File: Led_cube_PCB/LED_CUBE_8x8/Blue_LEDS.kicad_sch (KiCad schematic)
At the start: 101 parts, among them IC13 74AHCT244PW,118, IC14 74AHCT244PW,118, IC15 74AHCT244PW,118, IC17 74AHCT244PW,118, IC18 74AHCT244PW,118, IC23 74AHCT244PW,118, IC24 74AHCT244PW,118, IC25 74AHCT244PW,118, IC27 SN74HCS238DYYR, J7 Conn_02x16_Odd_Even, J8 Conn_02x16_Odd_Even

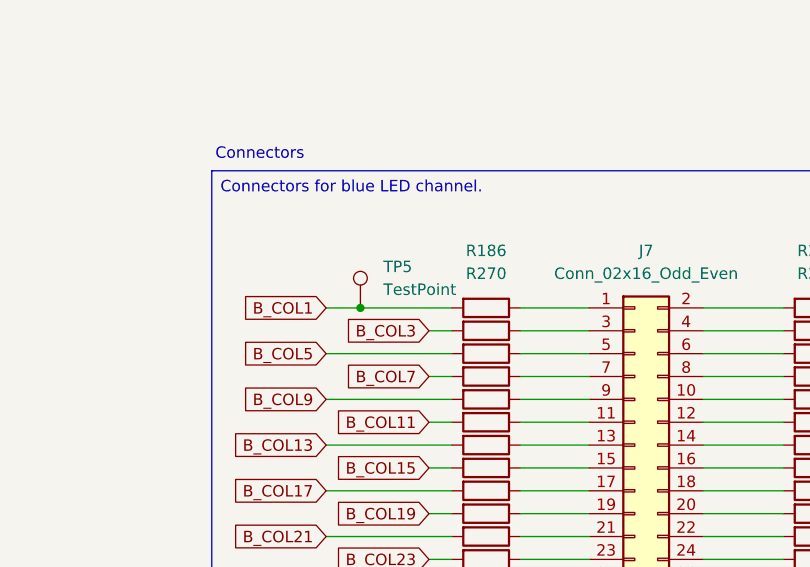
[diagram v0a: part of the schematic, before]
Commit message: Finalized schematic changed power source and buck converter due to unavailability stock mouser. Also assigned all the footprints to all components and ran ERC.
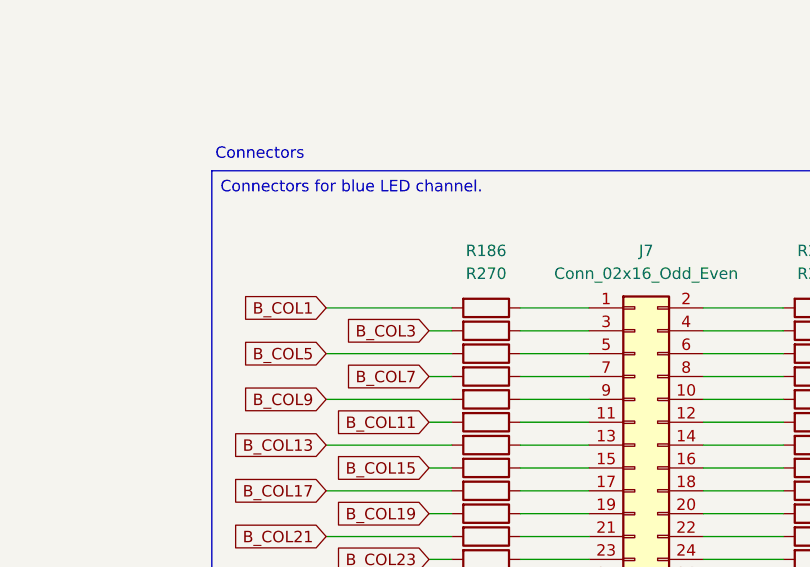
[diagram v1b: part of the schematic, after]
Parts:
- removed TP5: TestPoint, TestPoint:TestPoint_Pad_D2.0mm, symbol Connector:TestPoint
- C12, C14, C15, C20, C21, C22, C23, C24: footprint (none) -> Capacitor_SMD:C_0805_2012Metric_Pad1.18x1.45mm_HandSolder
- IC13, IC14, IC15, IC17, IC18, IC23, IC24, IC25: footprint SOP65P640X110-20N -> SamacSys_Parts:SOP65P640X110-20N
- IC27: footprint SOP50P326X110-16N -> SamacSys_Parts:SOP50P326X110-16N
- R186, R187, R188, R189, R190, R191, R192, R193, R194, R195, R196, R197, R198, R199, R200, R201, R202, R203, R204, R205, R206, R207, R208, R209, R210, R211, R212, R213, R214, R215, R216, R217, R218, R219, R220, R221, R222, R223, R224, R225, R226, R227, R228, R229, R230, R231, R232, R233, R234, R235, R236, R237, R238, R239, R240, R241, R242, R243, R244, R245, R246, R247, R248, R249, R26, R27, R28, R29, R3, R30, R33, R34, R35, R36, R45, R46, R47, R48, R49, R50, R51: footprint (none) -> Resistor_SMD:R_0805_2012Metric_Pad1.20x1.40mm_HandSolder

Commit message: start of PCB layout
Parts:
- removed R30, R33, R34, R35, R48, R49, R50, R51: R10K, Resistor_SMD:R_0805_2012Metric_Pad1.20x1.40mm_HandSolder, symbol Device:R
- C12, C14, C15, C20, C21, C22, C23, C24: footprint Capacitor_SMD:C_0805_2012Metric_Pad1.18x1.45mm_HandSolder -> Capacitor_SMD:C_0603_1608Metric_Pad1.08x0.95mm_HandSolder
- R186, R187, R188, R189, R190, R191, R192, R193, R194, R195, R196, R197, R198, R199, R200, R201, R202, R203, R204, R205, R206, R207, R208, R209, R210, R211, R212, R213, R214, R215, R216, R217, R218, R219, R220, R221, R222, R223, R224, R225, R226, R227, R228, R229, R230, R231, R232, R233, R234, R235, R236, R237, R238, R239, R240, R241, R242, R243, R244, R245, R246, R247, R248, R249, R26, R27, R28, R29, R3, R36, R45, R46, R47: footprint Resistor_SMD:R_0805_2012Metric_Pad1.20x1.40mm_HandSolder -> Resistor_SMD:R_0603_1608Metric_Pad0.98x0.95mm_HandSolder

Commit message: Top layer placement done revised the SWD connector and started routing.
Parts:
- J7, J8: footprint Connector_PinHeader_1.00mm:PinHeader_2x16_P1.00mm_Vertical -> Connector_PinSocket_2.54mm:PinSocket_2x16_P2.54mm_Vertical
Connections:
- net +5V: now also C24.1; no longer C24.2
- net GND: now also C24.2; no longer C24.1
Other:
- moved on the sheet: C24
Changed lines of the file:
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@@
 	(symbol
 		(lib_id "Device:C")
-		(at 210.82 85.09 0)
+		(at 210.82 85.09 180)
 		(unit 1)
 		(body_style 1)
@@
 					(size 1.27 1.27)
 				)
-				(justify left)
+				(justify right)
 			)
 		)
@@
 					(size 1.27 1.27)
 				)
-				(justify left)
+				(justify right)
 			)
 		)
 		(property "Footprint" "Capacitor_SMD:C_0603_1608Metric_Pad1.08x0.95mm_HandSolder"
-			(at 211.7852 88.9 0)
+			(at 209.8548 81.28 0)
 			(hide yes)
 			(show_name no)
@@
 			)
 		)
-		(property "Footprint" "Connector_PinHeader_1.00mm:PinHeader_2x16_P1.00mm_Vertical"
+		(property "Footprint" "Connector_PinSocket_2.54mm:PinSocket_2x16_P2.54mm_Vertical"
 			(at 334.01 118.11 0)
 			(hide yes)
@@
 			)
 		)
-		(property "Footprint" "Connector_PinHeader_1.00mm:PinHeader_2x16_P1.00mm_Vertical"
+		(property "Footprint" "Connector_PinSocket_2.54mm:PinSocket_2x16_P2.54mm_Vertical"
 			(at 334.01 168.91 0)
 			(hide yes)
@@
 		(instances
 			(project "LED_CUBE_8x8"
+				(path "/b239677e-e361-4439-8200-63fb41f7e03c/028ca277-4d5d-4d09-af7b-5a73ce3cf523"
+					(reference "IC13")
+					(unit 1)
+				)
 				(path "/b239677e-e361-4439-8200-63fb41f7e03c/cc8bd84f-da41-4d1f-b6a9-e2091cdfadf0"
 					(reference "IC13")
